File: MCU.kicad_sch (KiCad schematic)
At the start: 23 parts, among them SW1 SW_Push_Shielded, U1 STM32F407VGTx, Y1 26Mhz

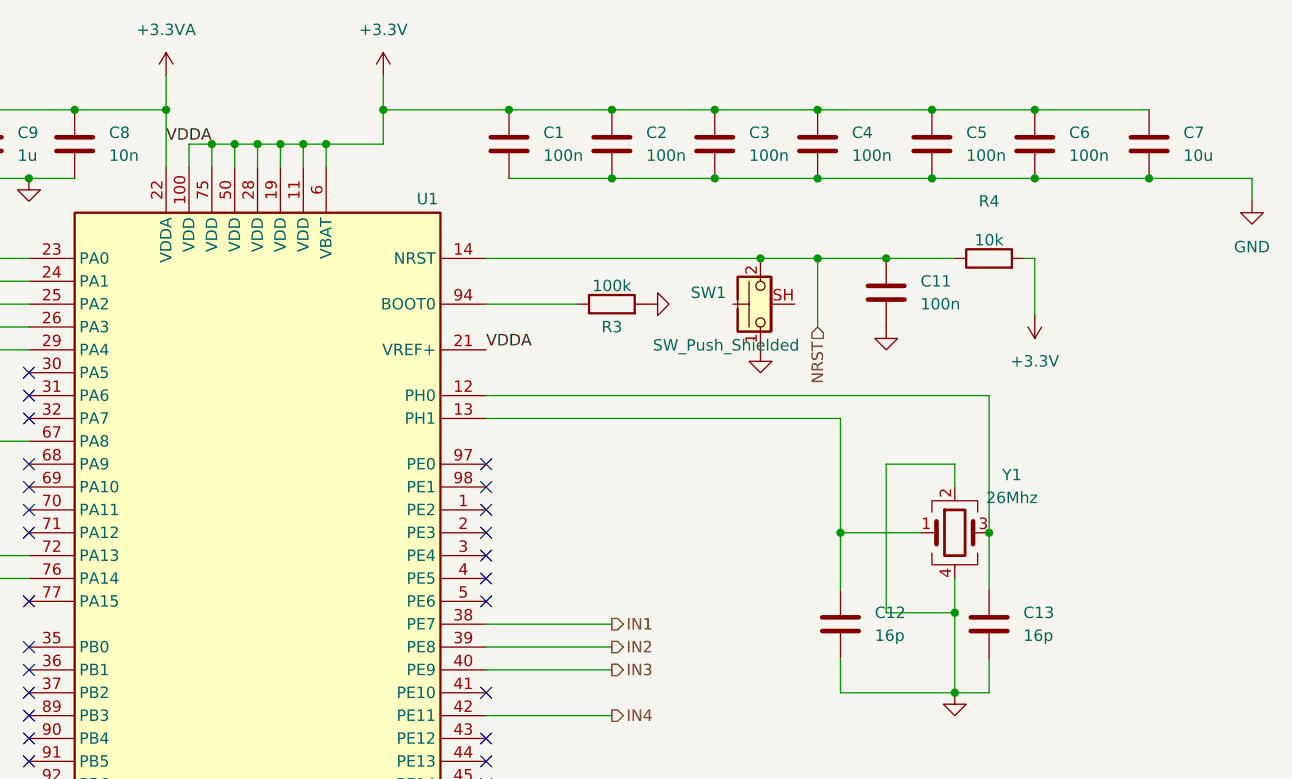
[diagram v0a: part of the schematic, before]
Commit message: Added Footprint
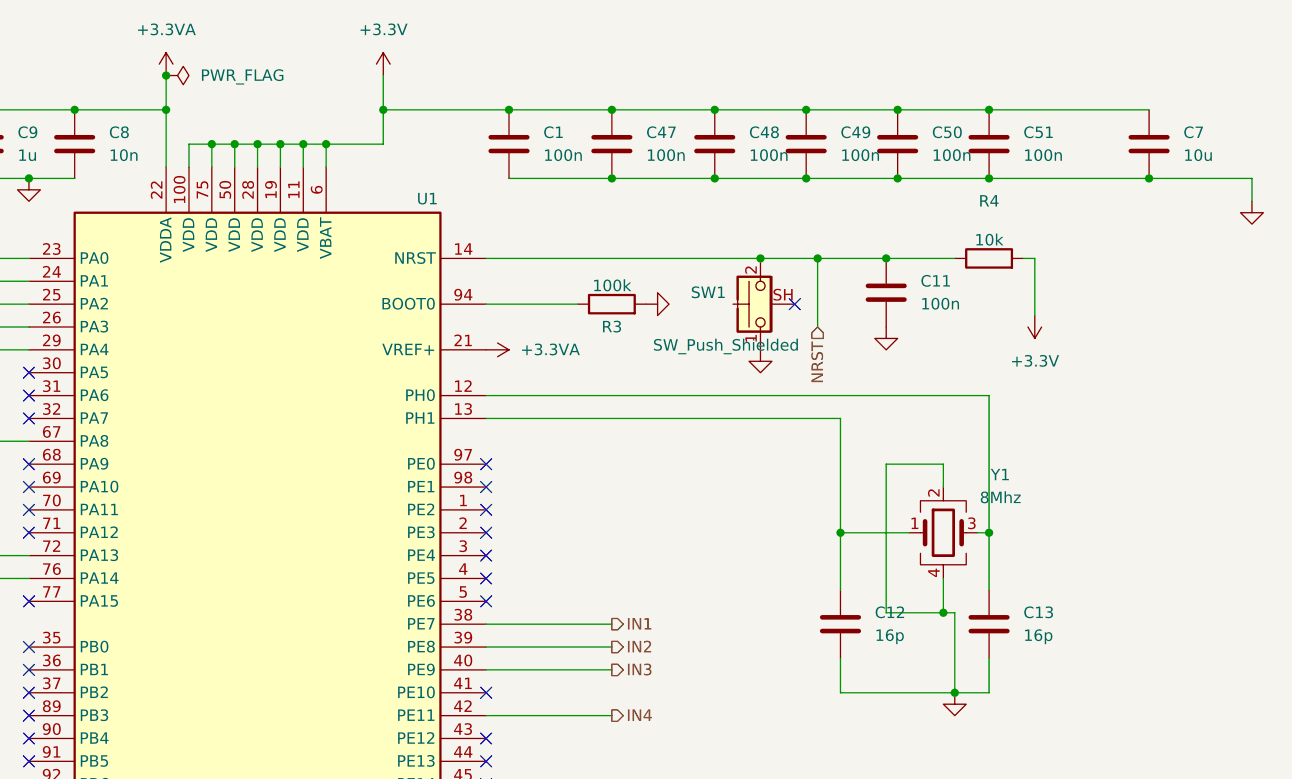
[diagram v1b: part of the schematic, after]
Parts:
- removed C2, C3, C4, C5, C6: 100n, Capacitor_SMD:C_0603_1608Metric_Pad1.08x0.95mm_HandSolder, symbol Device:C
- added C47, C48, C49, C50, C51: 100n, Capacitor_SMD:C_0805_2012Metric_Pad1.18x1.45mm_HandSolder, symbol Device:C
- C1, C11, C15: footprint Capacitor_SMD:C_0603_1608Metric_Pad1.08x0.95mm_HandSolder -> Capacitor_SMD:C_0805_2012Metric_Pad1.18x1.45mm_HandSolder
- C10, C7, C9: footprint Capacitor_SMD:C_0603_1608Metric_Pad1.08x0.95mm_HandSolder -> Capacitor_SMD:C_1206_3216Metric_Pad1.33x1.80mm_HandSolder
- R3, R4: footprint (none) -> Resistor_SMD:R_0805_2012Metric_Pad1.20x1.40mm_HandSolder
- Y1: value 26Mhz -> 8Mhz; footprint (none) -> Crystal:Crystal_HC33-U_Vertical
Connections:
- net +3.3V: now also C47.1, C48.1, C49.1, C50.1, C51.1
- net GND: now also C47.2, C48.2, C49.2, C50.2, C51.2
- no-connect marks 64 -> 65
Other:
- moved on the sheet: Y1

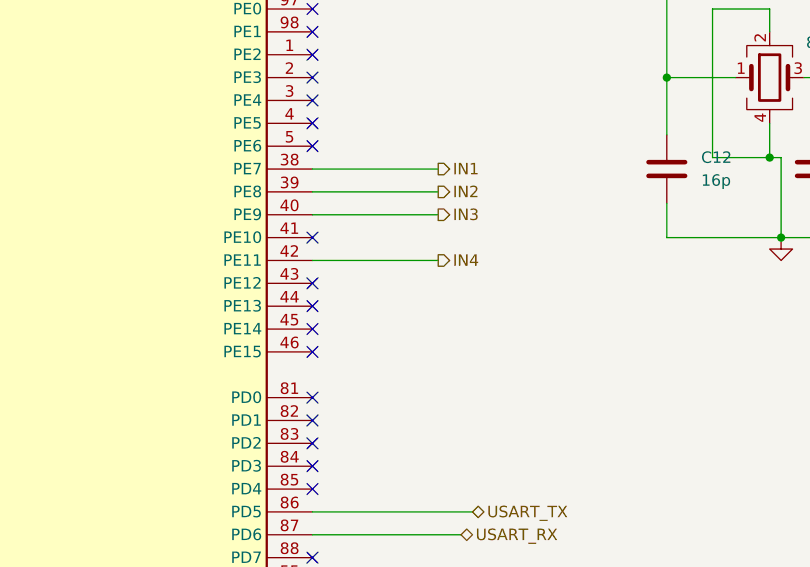
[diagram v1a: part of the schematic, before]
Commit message: Added a Relay Circuit
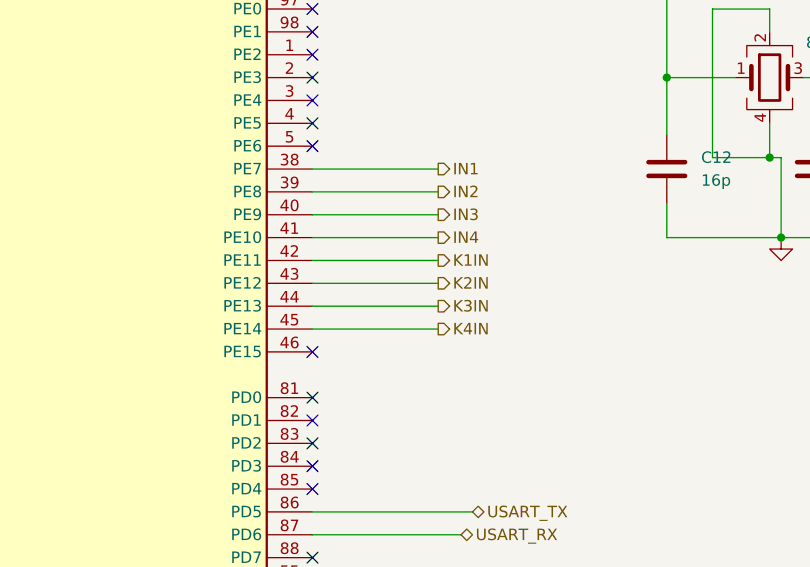
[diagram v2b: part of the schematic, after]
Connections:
- net IN4: now also U1.41 (PE10); no longer U1.42 (PE11)
- net K2IN: now reaches U1.43 (PE12)
- net K3IN: now reaches U1.44 (PE13)
- net K4IN: now reaches U1.45 (PE14)
- new net K1IN: U1.42 (PE11)
- no-connect marks 65 -> 61

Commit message: FInal Changes in Schgematic
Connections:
- net +3.3V renamed +3.3

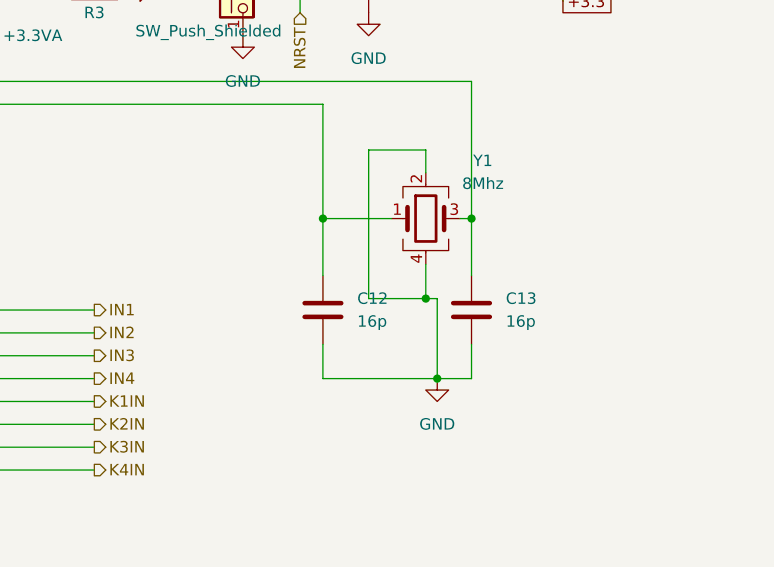
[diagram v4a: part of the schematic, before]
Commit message: Fixed the Silkscreen issue
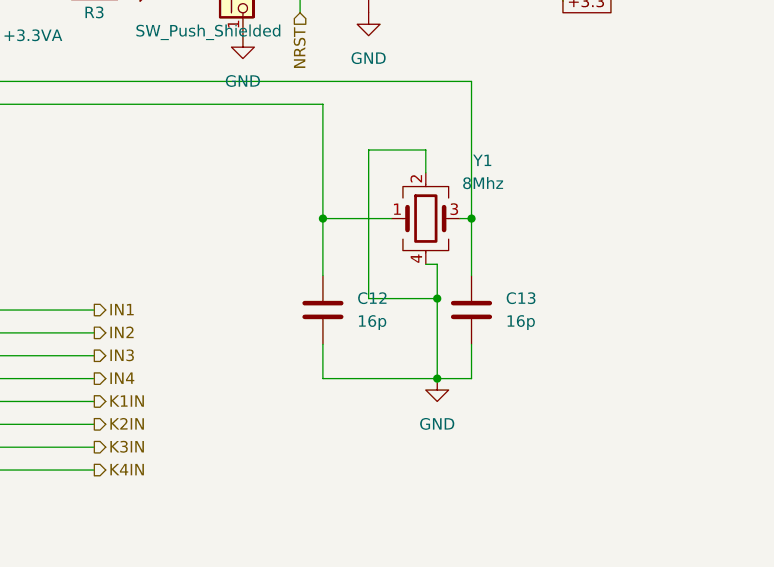
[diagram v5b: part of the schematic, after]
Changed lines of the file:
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@@
 	)
 	(junction
-		(at 195.58 87.63)
+		(at 196.85 87.63)
 		(diameter 0)
 		(color 0 0 0 0)
@@
 	(wire
 		(pts
+			(xy 196.85 83.82) (xy 195.58 83.82)
+		)
+		(stroke
+			(width 0)
+			(type default)
+		)
+	)
+	(wire
+		(pts
 			(xy 64.77 55.88) (xy 93.98 55.88)
 		)
@@
 	(wire
 		(pts
-			(xy 195.58 87.63) (xy 196.85 87.63)
-		)
-		(stroke
-			(width 0)
-			(type default)
-		)
-	)
-	(wire
-		(pts
 			(xy 116.84 35.56) (xy 119.38 35.56)
 		)
@@
 	(wire
 		(pts
-			(xy 189.23 87.63) (xy 195.58 87.63)
+			(xy 189.23 87.63) (xy 196.85 87.63)
 		)
 		(stroke
@@
 	(wire
 		(pts
-			(xy 195.58 83.82) (xy 195.58 87.63)
-		)
-		(stroke
+			(xy 196.85 83.82) (xy 196.85 87.63)
+		)
+		(stroke

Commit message: Deleted Uneeded Portion
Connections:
- net I2C1_SCL: now also U1.47 (PB10); no longer U1.92 (PB6)
- net I2C1_SDA: now also U1.48 (PB11); no longer U1.93 (PB7)
- net IN1: now also U1.42 (PE11); no longer U1.38 (PE7)
- net IN2: now also U1.41 (PE10); no longer U1.39 (PE8)
- net IN3: now also U1.39 (PE8); no longer U1.40 (PE9)
- net IN4: now also U1.38 (PE7); no longer U1.41 (PE10)
- net K1IN: now also U1.43 (PE12); no longer U1.42 (PE11)
- net K2IN: now also U1.44 (PE13); no longer U1.43 (PE12)
- net K3IN: now also U1.45 (PE14); no longer U1.44 (PE13)
- net K4IN: now also U1.46 (PE15); no longer U1.45 (PE14)
- net PWM1: now also U1.40 (PE9); no longer U1.67 (PA8)
- net ADC2: no longer names the net of U1.26 (PA3)
- net SINE_WAVE: no longer names the net of U1.29 (PA4)
- no-connect marks 61 -> 63

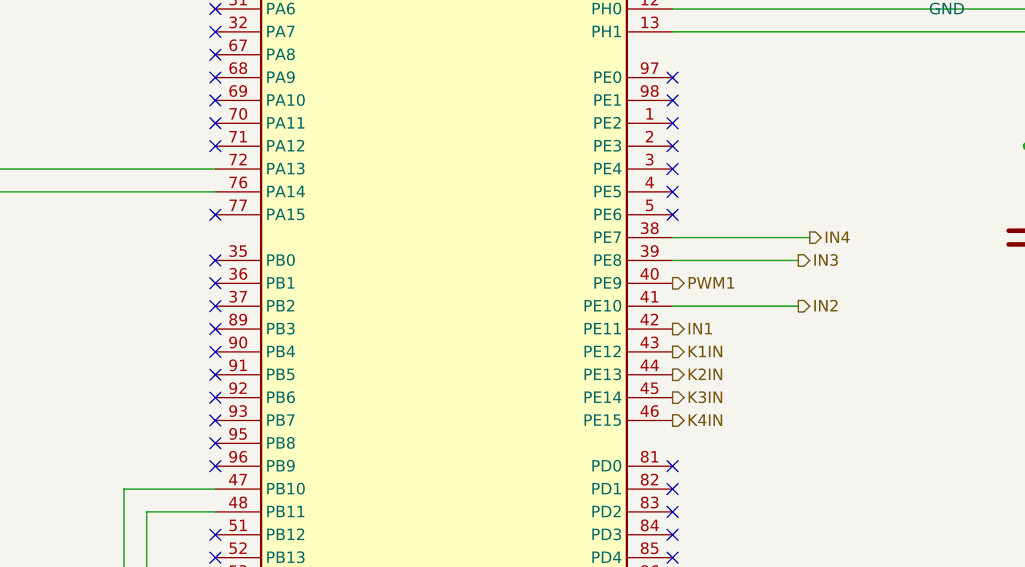
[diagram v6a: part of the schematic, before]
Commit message: Used Zones and Net
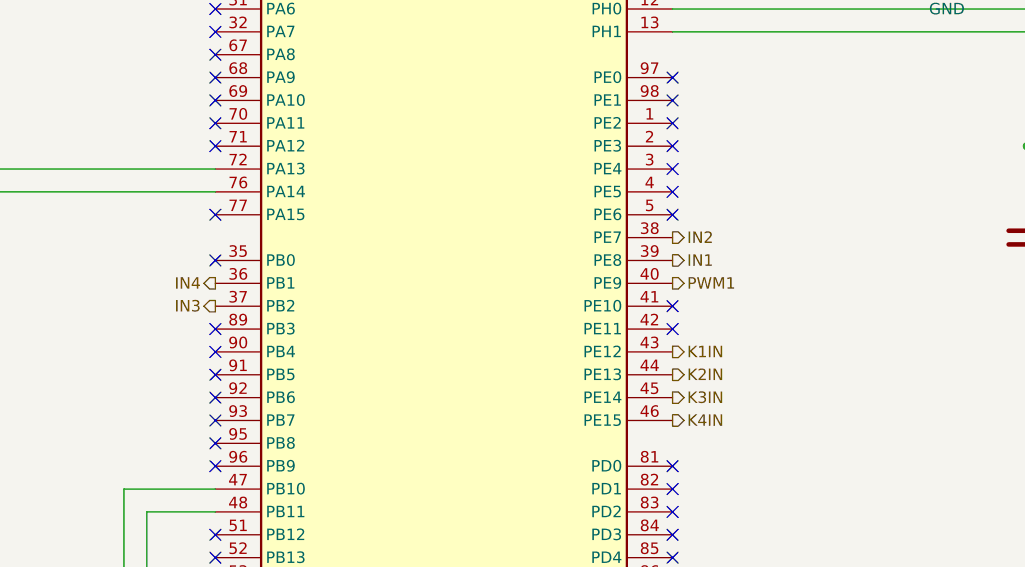
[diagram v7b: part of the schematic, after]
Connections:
- net IN1: now also U1.39 (PE8); no longer U1.42 (PE11)
- net IN2: now also U1.38 (PE7); no longer U1.41 (PE10)
- net IN3: now also U1.37 (PB2); no longer U1.39 (PE8)
- net IN4: now also U1.36 (PB1); no longer U1.38 (PE7)
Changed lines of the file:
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@@
-	)
-	(no_connect
-		(at 93.98 93.98)
 	)
 	(no_connect
@@
 	)
 	(no_connect
+		(at 144.78 96.52)
+	)
+	(no_connect
 		(at 144.78 147.32)
 	)
 	(no_connect
-		(at 93.98 96.52)
-	)
-	(no_connect
 		(at 93.98 157.48)
 	)
@@
 	)
 	(no_connect
+		(at 144.78 99.06)
+	)
+	(no_connect
 		(at 93.98 63.5)
 	)
@@
 	(wire
 		(pts
-			(xy 144.78 91.44) (xy 158.75 91.44)
-		)
-		(stroke
-			(width 0)
-			(type default)
-		)
-	)
-	(wire
-		(pts
-			(xy 144.78 88.9) (xy 160.02 88.9)
-		)
-		(stroke
-			(width 0)
-			(type default)
-		)
-	)
-	(wire
-		(pts
 			(xy 114.3 35.56) (xy 111.76 35.56)
 		)
@@
 		(pts
 			(xy 62.23 25.4) (xy 62.23 27.94)
-		)
-		(stroke
-			(width 0)
-			(type default)
-		)
-	)
-	(wire
-		(pts
-			(xy 144.78 96.52) (xy 158.75 96.52)
 		)
 		(stroke
@@
 		)
 	)
-	(hierarchical_label "IN3"
+	(hierarchical_label "IN1"
 		(shape output)
-		(at 158.75 91.44 0)
+		(at 144.78 91.44 0)
 		(effects
 			(font
@@
 		)
 	)
+	(hierarchical_label "IN4"
+		(shape output)
+		(at 93.98 93.98 180)
+		(effects
+			(font
+				(size 1.27 1.27)
+			)
+			(justify right)
+		)
+	)
 	(hierarchical_label "USART_TX"
 		(shape bidirectional)
@@
 		)
 	)
-	(hierarchical_label "IN4"
-		(shape output)
-		(at 160.02 88.9 0)
-		(effects
-			(font
-				(size 1.27 1.27)
-			)
-			(justify left)
-		)
-	)
 	(hierarchical_label "K4IN"
 		(shape output)
@@
 		)
 	)
-	(hierarchical_label "IN1"
-		(shape output)
-		(at 144.78 99.06 0)
-		(effects
-			(font
-				(size 1.27 1.27)
-			)
-			(justify left)
-		)
-	)
 	(hierarchical_label "K3IN"
 		(shape output)
@@
 		)
 	)
+	(hierarchical_label "IN2"
+		(shape output)
+		(at 144.78 88.9 0)
+		(effects
+			(font
+				(size 1.27 1.27)
+			)
+			(justify left)
+		)
+	)
 	(hierarchical_label "I2C1_SDA"
 		(shape bidirectional)
@@
 		)
 	)
-	(hierarchical_label "IN2"
+	(hierarchical_label "IN3"
 		(shape output)
-		(at 158.75 96.52 0)
-		(effects
-			(font
-				(size 1.27 1.27)
-			)
-			(justify left)
-		)
-	)
+		(at 93.98 96.52 180)
+		(effects
+			(font
+				(size 1.27 1.27)
+			)
+			(justify right)
+		)
+	)
